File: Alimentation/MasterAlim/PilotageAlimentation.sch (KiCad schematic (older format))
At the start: 7 parts, among them J4 INHIBIT, J5 ToRegul, U1 74LVC1G02

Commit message: Rework suite point robot
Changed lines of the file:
@@
 $Descr A4 11693 8268
 encoding utf-8
-Sheet 4 6
+Sheet 6 6
 Title ""
 Date ""
@@
 AR Path="/602E5F64/601CFDAA" Ref="J8"  Part="1"
 AR Path="/602E5F6A/601CFDAA" Ref="J12"  Part="1"
-F 0 "J6" H 3938 2445 50  0000 C CNN
+F 0 "J12" H 3938 2445 50  0000 C CNN
 F 1 "INHIBIT" H 3938 2536 50  0000 C CNN
 F 2 "TerminalBlock_Phoenix:TerminalBlock_Phoenix_MPT-0,5-2-2.54_1x02_P2.54mm_Horizontal" H 4020 2770 50  0001 C CNN
@@
 AR Path="/602E5F64/601CFDB7" Ref="U3"  Part="1"
 AR Path="/602E5F6A/601CFDB7" Ref="U4"  Part="1"
-F 0 "U2" H 5690 3860 50  0000 C CNN
+F 0 "U4" H 5690 3860 50  0000 C CNN
 F 1 "74LVC1G02" H 5850 3790 50  0000 C CNN
 F 2 "Package_TO_SOT_SMD:SOT-23-5_HandSoldering" H 5520 3660 50  0001 C CNN
@@
 AR Path="/602E5F64/601CFDCE" Ref="C8"  Part="1"
 AR Path="/602E5F6A/601CFDCE" Ref="C10"  Part="1"
-F 0 "C6" H 5895 2726 50  0000 L CNN
+F 0 "C10" H 5895 2726 50  0000 L CNN
 F 1 "100n" H 5895 2635 50  0000 L CNN
 F 2 "Capacitor_SMD:C_0603_1608Metric_Pad1.08x0.95mm_HandSolder" H 5818 2530 50  0001 C CNN
@@
 AR Path="/602E5F64/601CFDD6" Ref="C7"  Part="1"
 AR Path="/602E5F6A/601CFDD6" Ref="C9"  Part="1"
-F 0 "C3" H 5495 2726 50  0000 L CNN
+F 0 "C9" H 5495 2726 50  0000 L CNN
 F 1 "1u" H 5495 2635 50  0000 L CNN
 F 2 "Capacitor_SMD:CP_Elec_4x5.3" H 5380 2680 50  0001 C CNN
@@
 AR Path="/602E5F64/601E718F" Ref="J9"  Part="1"
 AR Path="/602E5F6A/601E718F" Ref="J13"  Part="1"
-F 0 "J7" H 4100 3422 50  0000 L CNN
+F 0 "J13" H 4100 3422 50  0000 L CNN
 F 1 "ToRegul" H 4100 3331 50  0000 L CNN
 F 2 "TerminalBlock_Phoenix:TerminalBlock_Phoenix_MKDS-1,5-2-5.08_1x02_P5.08mm_Horizontal" H 4020 3430 50  0001 C CNN
@@
 AR Path="/602E5F64/602A722E" Ref="D6"  Part="1"
 AR Path="/602E5F6A/602A722E" Ref="D8"  Part="1"
-F 0 "D5" V 6694 3202 50  0000 R CNN
+F 0 "D8" V 6694 3202 50  0000 R CNN
 F 1 "ENABLE REGUL" V 6603 3202 50  0000 R CNN
 F 2 "LED_SMD:LED_0805_2012Metric" H 6610 3320 50  0001 C CNN
@@
 AR Path="/602E5F64/602A7235" Ref="R7"  Part="1"
 AR Path="/602E5F6A/602A7235" Ref="R8"  Part="1"
-F 0 "R6" H 6678 3066 50  0000 L CNN
+F 0 "R8" H 6678 3066 50  0000 L CNN
 F 1 "150" H 6678 2975 50  0000 L CNN
 F 2 "Resistor_SMD:R_0805_2012Metric_Pad1.20x1.40mm_HandSolder" V 6650 3010 50  0001 C CNN

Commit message: Finalisation alimentations
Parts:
- removed C1: 1u, Capacitor_SMD:CP_Elec_4x5.3, symbol Device:CP1
- removed J5: ToRegul, TerminalBlock_Phoenix:TerminalBlock_Phoenix_MKDS-1,5-2-5.08_1x02_P5.08mm_Horizontal, symbol Connector:Screw_Terminal_01x02
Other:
- moved on the sheet: C10, D8, J12, R8, U4

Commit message: Finalisation pour commande pack Alimentation 14/02/2021
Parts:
- C2: LCSC Part C80516 -> C14663; Tension 16V -> 50V
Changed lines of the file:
@@
 $Descr A4 11693 8268
 encoding utf-8
-Sheet 6 6
+Sheet 3 6
 Title ""
 Date ""
@@
 AR Path="/602E5F64/601CFDAA" Ref="J8"  Part="1"
 AR Path="/602E5F6A/601CFDAA" Ref="J12"  Part="1"
-F 0 "J12" H 6488 3585 50  0000 C CNN
+F 0 "J4" H 6488 3585 50  0000 C CNN
 F 1 "INHIBIT" H 6488 3676 50  0000 C CNN
 F 2 "TerminalBlock_Phoenix:TerminalBlock_Phoenix_MPT-0,5-2-2.54_1x02_P2.54mm_Horizontal" H 6570 3910 50  0001 C CNN
@@
 AR Path="/602E5F64/601CFDB7" Ref="U3"  Part="1"
 AR Path="/602E5F6A/601CFDB7" Ref="U4"  Part="1"
-F 0 "U4" H 4920 4080 50  0000 C CNN
+F 0 "U1" H 4920 4080 50  0000 C CNN
 F 1 "74LVC1G02" H 5080 4010 50  0000 C CNN
 F 2 "Package_TO_SOT_SMD:SOT-23-5_HandSoldering" H 4750 3880 50  0001 C CNN
@@
 AR Path="/602E5F64/601CFDCE" Ref="C8"  Part="1"
 AR Path="/602E5F6A/601CFDCE" Ref="C10"  Part="1"
-F 0 "C10" H 3965 3916 50  0000 L CNN
+F 0 "C2" H 3965 3916 50  0000 L CNN
 F 1 "100n" H 3965 3825 50  0000 L CNN
 F 2 "Capacitor_SMD:C_0603_1608Metric_Pad1.08x0.95mm_HandSolder" H 3888 3720 50  0001 C CNN
 F 3 "~" H 3850 3870 50  0001 C CNN
-F 4 "C80516" H 3850 3870 50  0001 C CNN "LCSC Part"
-F 5 "16V" H 3850 3870 50  0001 C CNN "Tension"
+F 4 " C14663" H 3850 3870 50  0001 C CNN "LCSC Part"
+F 5 "50V" H 3850 3870 50  0001 C CNN "Tension"
 	1    3850 3870
 	1    0    0    -1
@@
 AR Path="/602E5F64/602A722E" Ref="D6"  Part="1"
 AR Path="/602E5F6A/602A722E" Ref="D8"  Part="1"
-F 0 "D8" V 5694 3942 50  0000 R CNN
+F 0 "D4" V 5694 3942 50  0000 R CNN
 F 1 "ENABLE REGUL" V 5603 3942 50  0000 R CNN
 F 2 "LED_SMD:LED_0805_2012Metric" H 5610 4060 50  0001 C CNN
@@
 AR Path="/602E5F64/602A7235" Ref="R7"  Part="1"
 AR Path="/602E5F6A/602A7235" Ref="R8"  Part="1"
-F 0 "R8" H 5678 3806 50  0000 L CNN
+F 0 "R5" H 5678 3806 50  0000 L CNN
 F 1 "150" H 5678 3715 50  0000 L CNN
 F 2 "Resistor_SMD:R_0805_2012Metric_Pad1.20x1.40mm_HandSolder" V 5650 3750 50  0001 C CNN

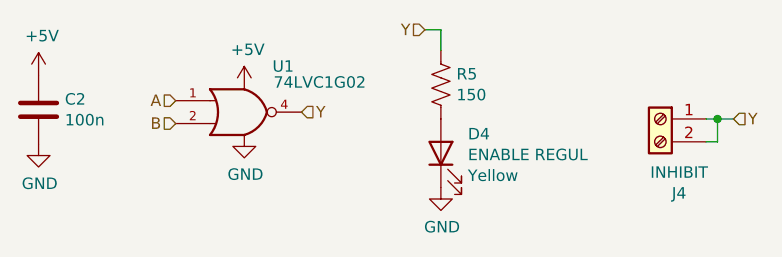
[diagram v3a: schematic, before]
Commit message: Fix Master Alim : affichage statut AU
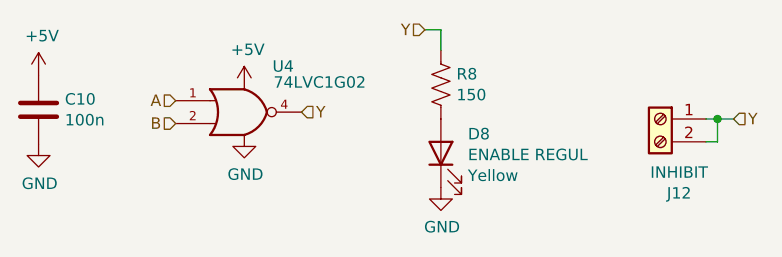
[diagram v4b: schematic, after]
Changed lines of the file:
@@
 AR Path="/602E5F64/601CFDAA" Ref="J8"  Part="1"
 AR Path="/602E5F6A/601CFDAA" Ref="J12"  Part="1"
-F 0 "J4" H 6488 3585 50  0000 C CNN
+F 0 "J12" H 6488 3585 50  0000 C CNN
 F 1 "INHIBIT" H 6488 3676 50  0000 C CNN
 F 2 "TerminalBlock_Phoenix:TerminalBlock_Phoenix_MPT-0,5-2-2.54_1x02_P2.54mm_Horizontal" H 6570 3910 50  0001 C CNN
@@
 AR Path="/602E5F64/601CFDB7" Ref="U3"  Part="1"
 AR Path="/602E5F6A/601CFDB7" Ref="U4"  Part="1"
-F 0 "U1" H 4920 4080 50  0000 C CNN
+F 0 "U4" H 4920 4080 50  0000 C CNN
 F 1 "74LVC1G02" H 5080 4010 50  0000 C CNN
 F 2 "Package_TO_SOT_SMD:SOT-23-5_HandSoldering" H 4750 3880 50  0001 C CNN
@@
 AR Path="/602E5F64/601CFDCE" Ref="C8"  Part="1"
 AR Path="/602E5F6A/601CFDCE" Ref="C10"  Part="1"
-F 0 "C2" H 3965 3916 50  0000 L CNN
+F 0 "C10" H 3965 3916 50  0000 L CNN
 F 1 "100n" H 3965 3825 50  0000 L CNN
 F 2 "Capacitor_SMD:C_0603_1608Metric_Pad1.08x0.95mm_HandSolder" H 3888 3720 50  0001 C CNN
@@
 AR Path="/602E5F64/602A722E" Ref="D6"  Part="1"
 AR Path="/602E5F6A/602A722E" Ref="D8"  Part="1"
-F 0 "D4" V 5694 3942 50  0000 R CNN
+F 0 "D8" V 5694 3942 50  0000 R CNN
 F 1 "ENABLE REGUL" V 5603 3942 50  0000 R CNN
 F 2 "LED_SMD:LED_0805_2012Metric" H 5610 4060 50  0001 C CNN
@@
 AR Path="/602E5F64/602A7235" Ref="R7"  Part="1"
 AR Path="/602E5F6A/602A7235" Ref="R8"  Part="1"
-F 0 "R5" H 5678 3806 50  0000 L CNN
+F 0 "R8" H 5678 3806 50  0000 L CNN
 F 1 "150" H 5678 3715 50  0000 L CNN
 F 2 "Resistor_SMD:R_0805_2012Metric_Pad1.20x1.40mm_HandSolder" V 5650 3750 50  0001 C CNN
